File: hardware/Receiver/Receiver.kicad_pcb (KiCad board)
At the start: 4 copper layers, 65 x 42 mm, 120 parts, among them J1 USB_C_Receptacle_USB2.0, J3 JST_PH, J4 Conn_01x04, Q1 2N7002, Q10 NChan, Q11 NChan, Q2 NChan, Q3 NChan, Q4 NChan, Q5 PChan, Q6 PChan, Q7 PChan, Q8 NChan, Q9 NChan, SW1 Reset, SW2 1825027-8, SW3 Boot, U1 TPS22810DRV, U2 DMG6602SVTQ, U3 DMG6602SVTQ, U4 TLV493DA1B6HTSA2, U5 TPS22810DRV, U6 AZ1117-3.3, U7 ESP32-S3-MINI-1-N8

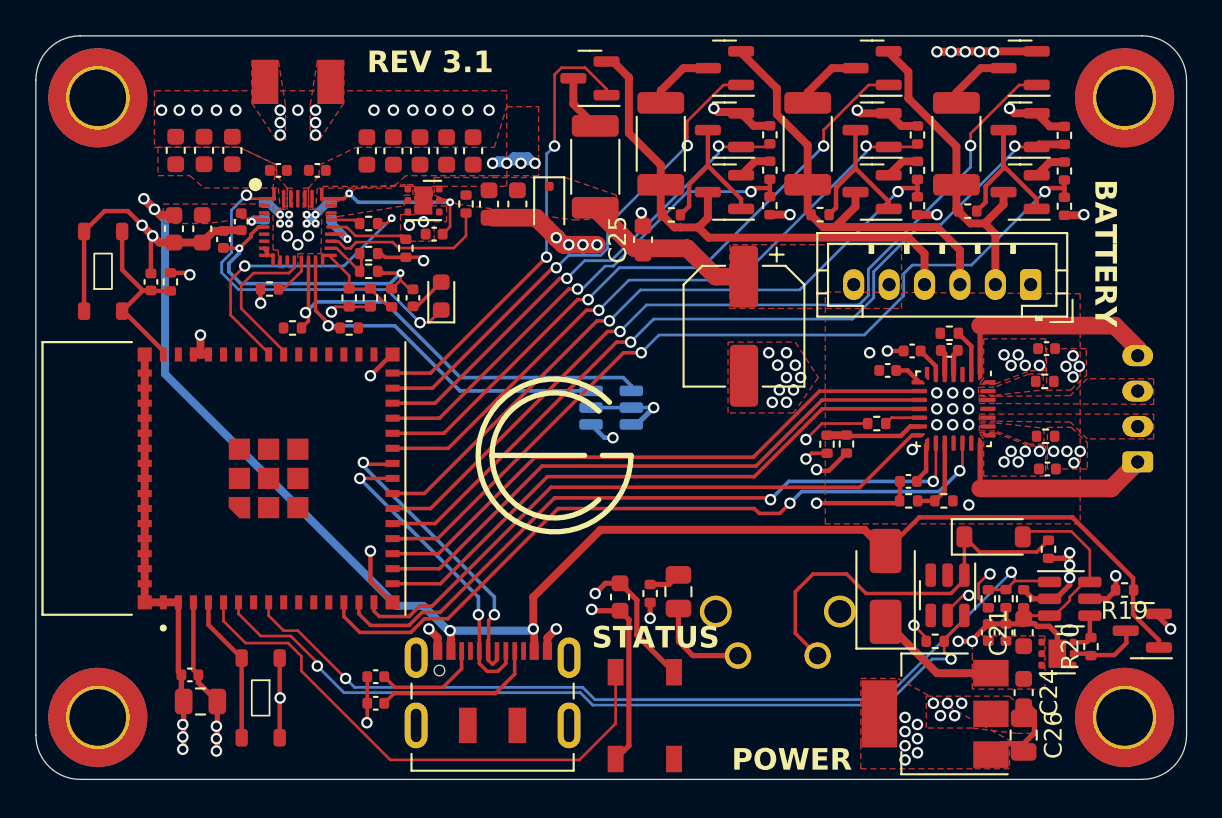
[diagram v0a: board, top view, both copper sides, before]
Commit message: add battery balancing IC
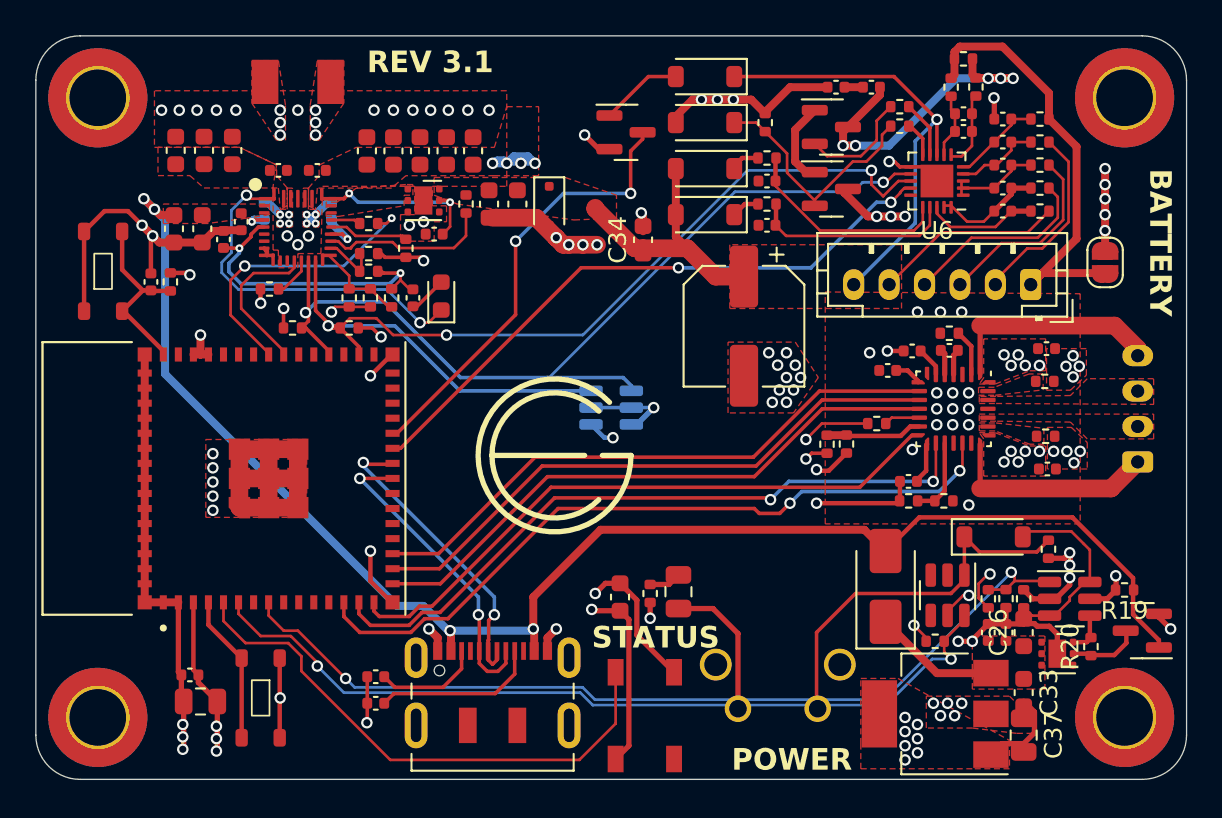
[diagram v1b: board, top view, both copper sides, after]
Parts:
- removed Q10, Q11, Q8, Q9: NChan, Package_TO_SOT_SMD:SOT-23
- removed Q5, Q6, Q7: PChan, Package_TO_SOT_SMD:SOT-23
- removed the R34 at (152.8, 85.1)
- removed the R35 at (161.1, 85.1)
- removed the R36 at (169.5, 85.1)
- added C21: 220nf, Capacitor_SMD:C_0402_1005Metric, F.Cu at (172.1, 88.9)
- added C22: 220nf, Capacitor_SMD:C_0402_1005Metric, F.Cu at (172.1, 87.6)
- added C23: 220nf, Capacitor_SMD:C_0402_1005Metric, F.Cu at (172.1, 86.3)
- added C24: 220nf, Capacitor_SMD:C_0402_1005Metric, F.Cu at (172.1, 85.0)
- added C25: 220nf, Capacitor_SMD:C_0402_1005Metric, F.Cu at (172.1, 83.7)
- added C28: 100p, Capacitor_SMD:C_0402_1005Metric, F.Cu at (169.9, 84.4)
- added C29: 0.1u, Capacitor_SMD:C_0402_1005Metric, F.Cu at (169.9, 83.4)
- added C30: 1u, Capacitor_SMD:C_0402_1005Metric, F.Cu at (158.8, 89.7)
- added C32: 1u, Capacitor_SMD:C_0402_1005Metric, F.Cu at (158.8, 87.2)
- added C35: 0.1u, Capacitor_SMD:C_0402_1005Metric, F.Cu at (164.7, 81.9)
- added C36: 0.1u, Capacitor_SMD:C_0402_1005Metric, F.Cu at (162.7, 81.9)
- added D10: 1N4148WQ-13-F, Diode_SMD:D_SOD-123, F.Cu at (155.3, 83.9)
- added D7: 1N4148WQ-13-F, Diode_SMD:D_SOD-123, F.Cu at (155.3, 89.1)
- added D8: 1N4148WQ-13-F, Diode_SMD:D_SOD-123, F.Cu at (155.3, 86.5)
- added D9: 1N4148WQ-13-F, Diode_SMD:D_SOD-123, F.Cu at (155.3, 81.3)
- added JP1: BQ76905_Bypass, Jumper:SolderJumper-2_P1.3mm_Open_RoundedPad1.0x1.5mm, F.Cu at (177.9, 91.8)
- added U6: ~, Package_DFN_QFN:UQFN-20-1EP_3x3mm_P0.4mm_EP1.85x1.85mm, F.Cu at (168.4, 87.2)
- Q2, Q3: value NChan -> NMOS
- Q4: value NChan -> PMOS
- R21, R22, R23, R24, R25: value 100k -> 10
- R26, R28: value 100k -> 100
- R27: value 282k -> 1m
- R29: value 155k -> 100
- R30: value 100k -> 0
- R31: value 28k -> 5.1k
- R32: value 100k -> 5.1k
- R33: value 400 -> 100k; footprint Resistor_SMD:R_2010_5025Metric -> Resistor_SMD:R_0402_1005Metric
- moved Q4 22.3 mm to (150.8, 84.5), turned to 0 degrees
- moved R24 21.2 mm to (174.2, 85.0), turned to 180 degrees
- moved R21 15.9 mm to (174.2, 88.9), turned to 180 degrees
- moved R25 13.5 mm to (174.2, 83.7), turned to 180 degrees
- moved R27 12.6 mm to (169.9, 80.3), turned to 0 degrees
- moved R32 10.3 mm to (166.3, 84.1), turned to 180 degrees
- moved R31 9.99 mm to (166.3, 83.0), turned to 180 degrees
- moved R33 9.92 mm to (158.7, 83.9), turned to -90 degrees
- moved R30 8.92 mm to (158.8, 85.9), turned to 0 degrees
- moved R22 7.54 mm to (174.2, 87.6), turned to 180 degrees
- moved R26 7.06 mm to (169.2, 81.9), turned to 90 degrees
- moved Q2 6.04 mm to (162.4, 84.2), turned to 0 degrees
- moved R29 5.75 mm to (170.6, 81.9), turned to 90 degrees
- moved Q3 4.04 mm to (162.4, 87.7), turned to 0 degrees
- moved SW3 3.00 mm to (157.2, 117.0)
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- renumbered C21 to C26, C22 to C27, C23 to C31, C24 to C33, C25 to C34, C26 to C37, C30 to C38, C27 to C39, C28 to C40, C29 to C41, C31 to C42, C32 to C43, C35 to C44, C34 to C45, C36 to C46, C33 to C47, R39 to R34, R40 to R35, R41 to R36, R46 to R37, R47 to R38, R37 to R39, R44 to R40, R45 to R41, R38 to R42, R42 to R43, R43 to R44, SW3 to SW2, SW2 to SW3, U6 to U7, U7 to U8
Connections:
- BQ25792RQMR1 pad 16: /TS -> Net-(BQ25792RQMR1-TS)
- J3 pad 1: GND -> /BAT_C0
- J3 pad 6: /TC -> /TS
- Q2 pad 1: /M2 -> Net-(Q2-D)
- Q2 pad 2: GND -> Net-(Q2-G)
- Q2 pad 3: Net-(Q2-D) -> Net-(Q2-S)
- Q3 pad 1: /M3 -> Net-(Q2-D)
- Q3 pad 2: GND -> Net-(D10-K)
- Q3 pad 3: Net-(Q3-D) -> GND
- Q4 pad 1: /M4 -> Net-(D9-A)
- Q4 pad 2: GND -> +3.3V
- Q4 pad 3: Net-(Q4-D) -> /WAKE
- R13 pad 2: /TS -> Net-(BQ25792RQMR1-TS)
- R14 pad 1: /TS -> Net-(BQ25792RQMR1-TS)
- R16 pad 1: /TS -> Net-(BQ25792RQMR1-TS)
- R21 pad 1: /M2 -> /BAT+
- R21 pad 2: GND -> /VC4
- R22 pad 1: /M3 -> /BAT_C3
- R22 pad 2: GND -> /VC3
- R23 pad 1: /M4 -> /BAT_C2
- R23 pad 2: GND -> /VC2
- R24 pad 1: /BAT_C3 -> /BAT_C1
- R24 pad 2: Net-(Q2-D) -> /VC1
- R25 pad 1: /BAT_C2 -> /BAT_C0
- R25 pad 2: Net-(Q3-D) -> /VC0
- R26 pad 1: /BAT_C1 -> Net-(U6-SRN)
- R26 pad 2: Net-(Q4-D) -> /BAT_C0
- R27 pad 1: Net-(Q5-S) -> /BAT_C0
- R27 pad 2: /S2 -> Net-(Q2-S)
- R28 pad 1: /S2 -> Net-(D7-K)
- R28 pad 2: GND -> Net-(U6-BAT)
- R29 pad 2: /S3 -> Net-(Q2-S)
- R30 pad 1: /S3 -> Net-(D8-K)
- R30 pad 2: GND -> Net-(U6-REGSRC)
- R31 pad 2: /S4 -> Net-(Q2-G)
- R32 pad 1: /S4 -> Net-(U6-CHG)
- R32 pad 2: GND -> Net-(D10-K)
- R33 pad 1: /BAT+ -> GND
- R33 pad 2: Net-(Q8-D) -> Net-(D10-K)
- U8 pad 16: /MS3 -> unconnected-(U8-IO12-Pad16)
- U8 pad 17: /MS2 -> unconnected-(U8-IO13-Pad17)
- U8 pad 18: /MS1 -> unconnected-(U8-IO14-Pad18)
- U8 pad 19: /S4 -> /MS3
- U8 pad 20: /M4 -> /MS2
- U8 pad 21: /C4 -> /MS1
- U8 pad 22: /S3 -> unconnected-(U8-IO18/DAC2-Pad22)
- U8 pad 25: /M3 -> /ALERT
- U8 pad 26: /C3 -> /WAKE
- U8 pad 27: /S2 -> unconnected-(U8-IO47-Pad27)
- U8 pad 28: /M2 -> unconnected-(U8-IO33-Pad28)
- U8 pad 29: /C2 -> unconnected-(U8-IO34-Pad29)
- U8 pad 30: /C1 -> unconnected-(U8-IO48-Pad30)
- U8 pad 32: unconnected-(U7-IO36-Pad32) -> /SDA
- U8 pad 33: unconnected-(U7-IO37-Pad33) -> /SCL
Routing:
- net /C4: track 48.4 -> 0.00 mm, vias 2 -> 0
- net /M4: track 47.9 -> 0.00 mm, vias 2 -> 0
- net /S4: track 47.8 -> 0.00 mm, vias 2 -> 0
- net /SDA: track 21.0 -> 61.8 mm, vias 1 -> 3
- net /S3: track 37.8 -> 0.00 mm, vias 2 -> 0
- net /M3: track 37.0 -> 0.00 mm, vias 2 -> 0
- net /C3: track 36.7 -> 0.00 mm, vias 2 -> 0
- net /ALERT: track 0.00 -> 35.5 mm, vias 0 -> 2
- net /C2: track 28.5 -> 0.00 mm, vias 2 -> 0
- net /S2: track 27.7 -> 0.00 mm, vias 2 -> 0
- net /M2: track 27.7 -> 0.00 mm, vias 2 -> 0
- net /SCL: track 24.9 -> 52.4 mm, vias 1 -> 2
- net GND: track 131.8 -> 158.2 mm, vias 94 -> 104
- net /C1: track 25.9 -> 0.00 mm, vias 2 -> 0
- net /WAKE: track 0.00 -> 25.2 mm, vias 0 -> 2
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
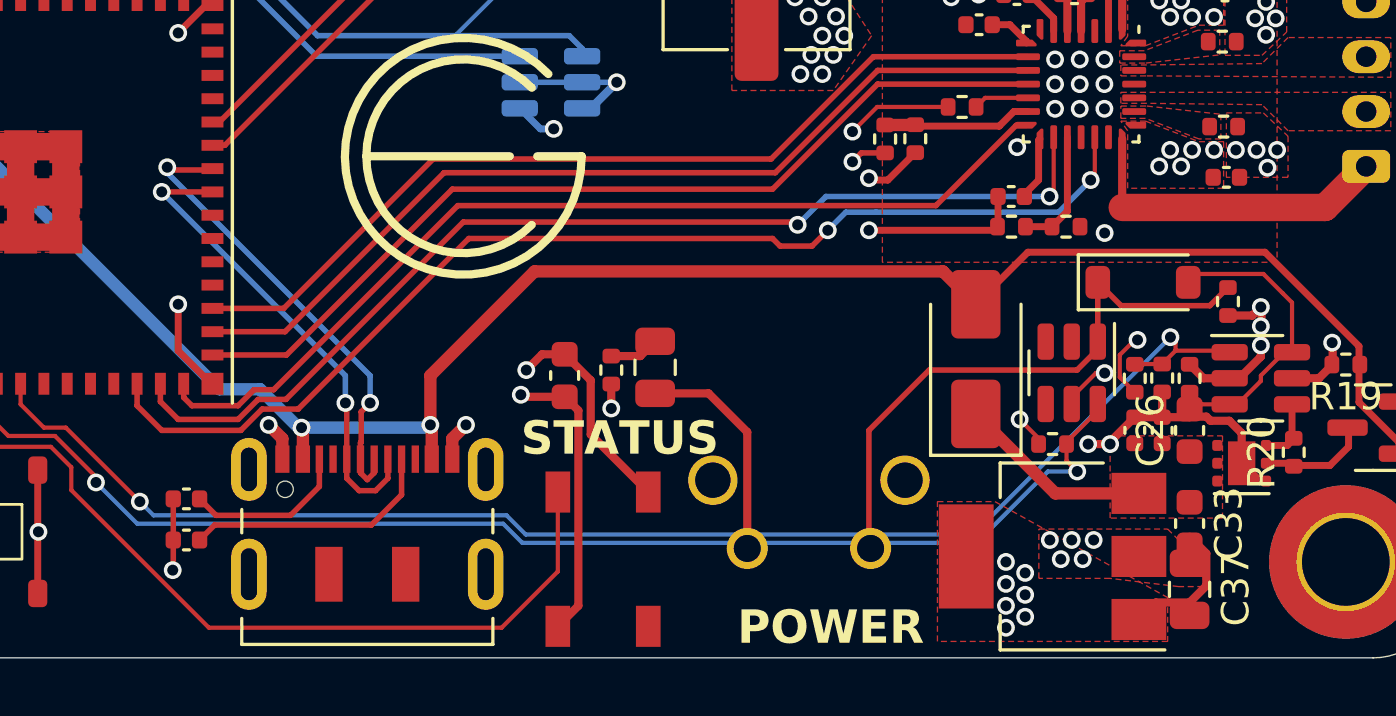
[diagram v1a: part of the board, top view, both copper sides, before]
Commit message: add tvs diodes
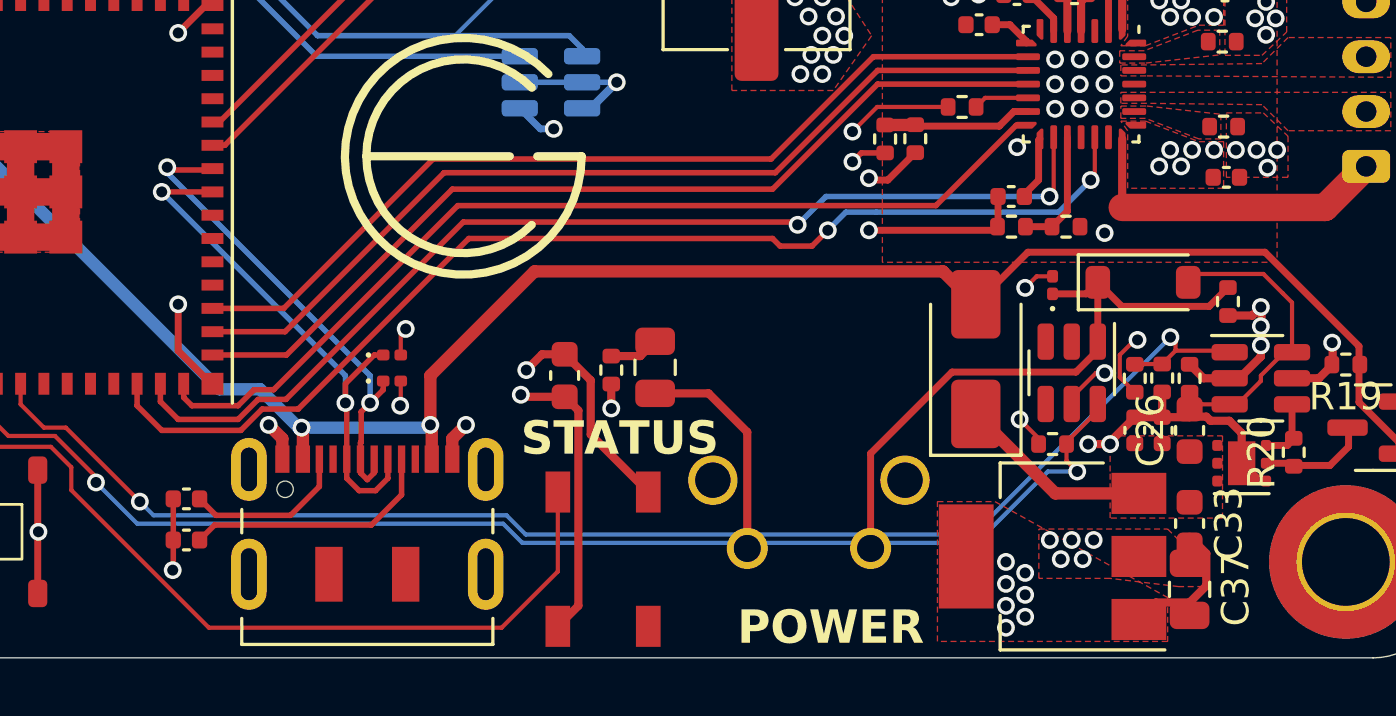
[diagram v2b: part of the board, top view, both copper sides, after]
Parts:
- added D11: ESD051-1F4, Diode_SMD:D_0201_0603Metric, F.Cu at (144.2, 110.0)
- added D12: ESD051-1F4, Diode_SMD:D_0201_0603Metric, F.Cu at (144.2, 110.9)
- added D13: ESD051-1F4, Diode_SMD:D_0201_0603Metric, F.Cu at (168.3, 107.4)
- U6: value ~ -> BQ76905
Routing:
- net GND: track 158.2 -> 161.3 mm, vias 104 -> 107
- net /D-: track 17.7 -> 20.2 mm
- net Net-(D13-A1): track 21.7 -> 23.0 mm
- net /D+: track 17.3 -> 18.3 mm

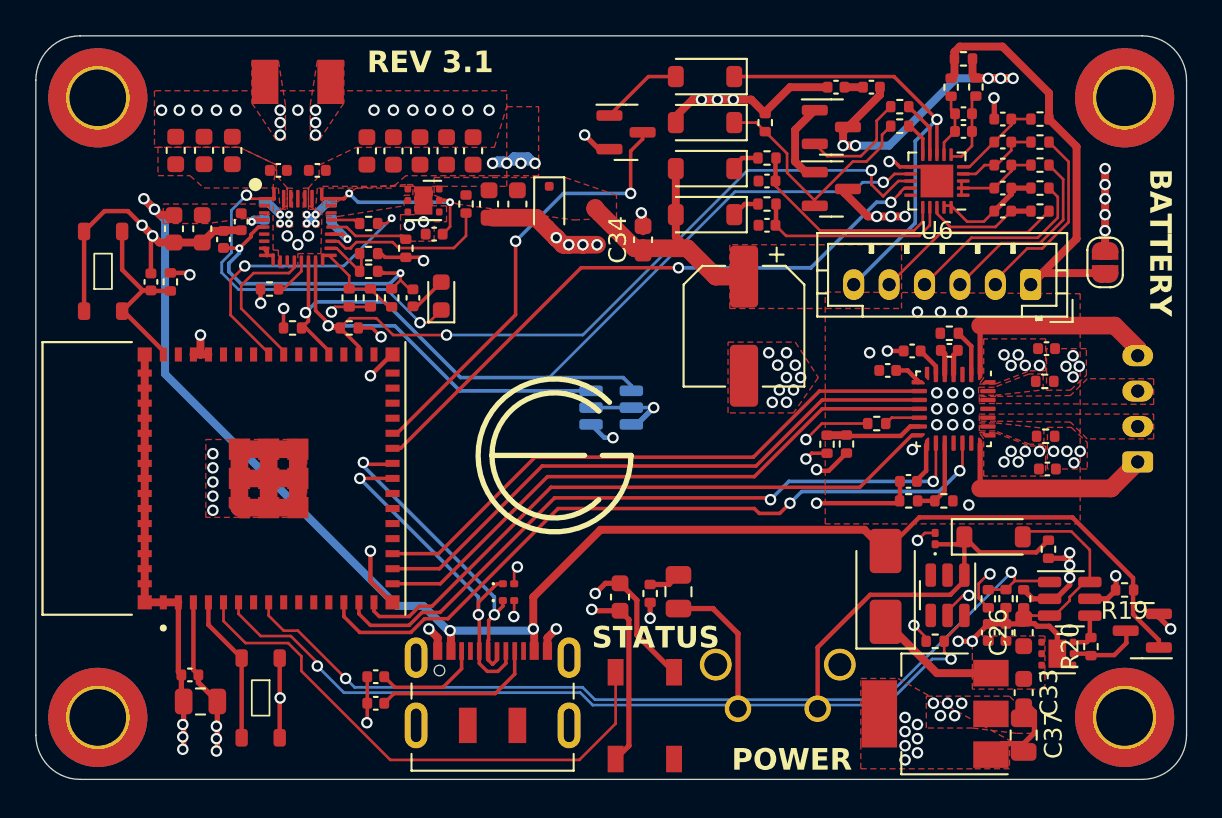
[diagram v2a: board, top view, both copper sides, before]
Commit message: add stitching vias
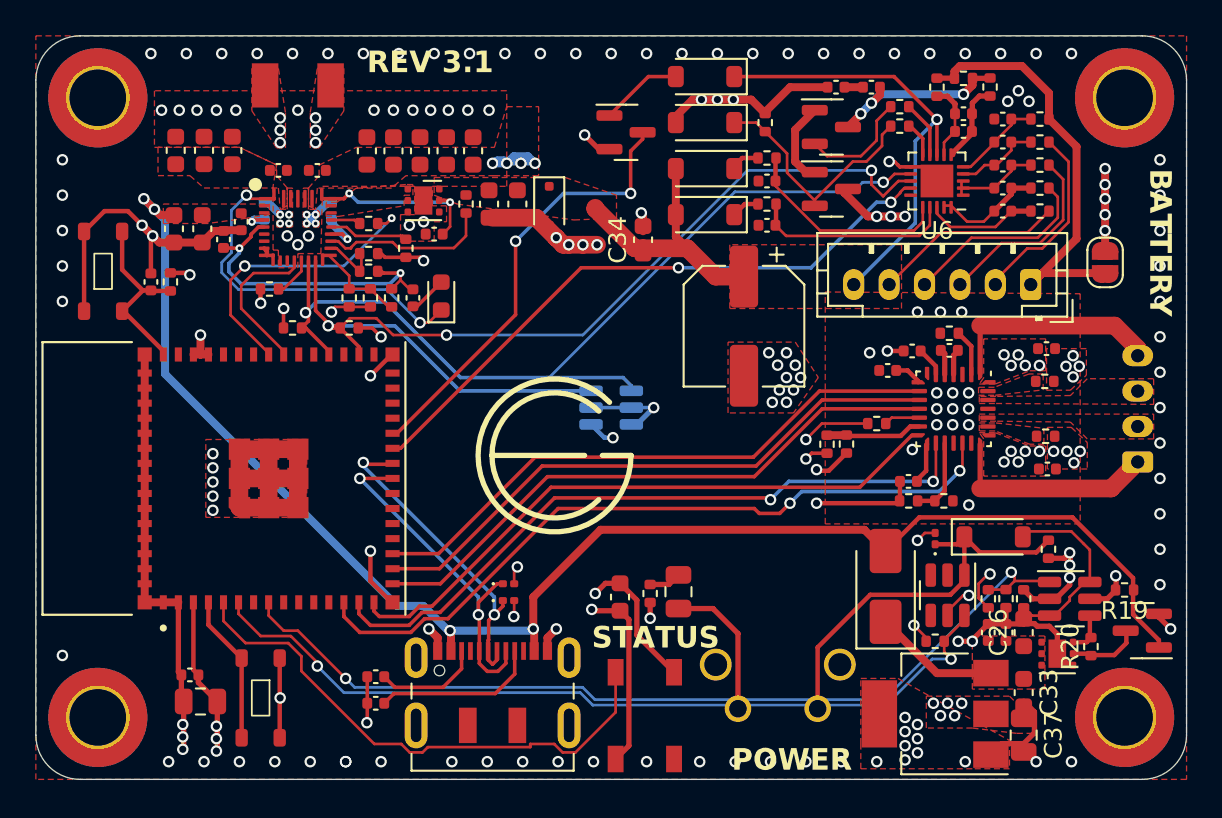
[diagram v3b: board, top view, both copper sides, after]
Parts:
- moved R27 1.10 mm to (169.9, 81.4)
- moved R29 0.80 mm to (171.4, 81.9)
- moved R26 0.80 mm to (168.4, 81.9)
- moved L1 0.20 mm to (132.3, 81.8)
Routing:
- net Net-(Q2-S): track 19.4 -> 10.5 mm, vias 5 -> 3
- net GND: track 161.3 -> 159.9 mm, vias 107 -> 174
- net Net-(U6-SRN): track 3.75 -> 4.43 mm
- net /BAT_C0: track 25.1 -> 24.5 mm
- net (no net): vias 0 -> 4

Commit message: update emc
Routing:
- net GND: vias 174 -> 222
- added copper zone on B.Cu, net GND

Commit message: create bom
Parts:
- moved C33 1.22 mm to (174.5, 115.9), turned to 0 degrees
- moved C37 0.63 mm to (173.9, 118.7)
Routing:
- net GND: track 159.9 -> 144.8 mm, vias 222 -> 223
- net /BAT_C1: track 10.7 -> 11.7 mm
- net /BAT_C0: track 24.5 -> 25.5 mm
- net Net-(U6-BAT): track 11.5 -> 12.5 mm
- net /VIN: track 7.15 -> 8.00 mm
- net /BAT_C2: track 10.8 -> 11.6 mm
- net /SHUTDOWN: track 51.9 -> 51.2 mm
- net /STAT: track 20.1 -> 20.8 mm
- net Net-(U6-REGSRC): track 12.1 -> 12.7 mm
- net /SW: track 47.3 -> 46.7 mm
- net /SW1: track 10.5 -> 11.0 mm

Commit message: PCB revision
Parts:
- removed C19, C20: 10u, Capacitor_SMD:C_0603_1608Metric
- added D14: TVN3V3B1S, Diode_SMD:D_0402_1005Metric, F.Cu at (124.6, 94.8)
- added D15: TVN3V3B1S, Diode_SMD:D_0402_1005Metric, F.Cu at (127.9, 113.7)
- added R45: 10k, Resistor_SMD:R_0402_1005Metric, F.Cu at (139.8, 103.6)
- C10, C12, C13, C15, C16, C17, C18, C2, C26, C3, C33, C34, C6: footprint Capacitor_SMD:C_0603_1608Metric -> Capacitor_SMD:C_0805_2012Metric
- D10, D4, D7, D8, D9: footprint Diode_SMD:D_SOD-123 -> Diode_SMD:D_SOD-323
- D11, D12, D13: value ESD051-1F4 -> TVN3V3B1S; footprint Diode_SMD:D_0201_0603Metric -> Diode_SMD:D_0402_1005Metric
- L1: footprint Inductor_SMD:L_Sunlord_MWSA0402S -> Inductor_SMD:L_1008_2520Metric
- R43, R44: footprint Resistor_SMD:R_0402_1005Metric -> Resistor_SMD:R_0603_1608Metric
- moved U2 2.55 mm to (177.7, 109.0)
- moved R20 2.10 mm to (177.0, 111.4), turned to 180 degrees
- moved D5 1.98 mm to (147.8, 87.1), turned to 90 degrees
- moved R19 1.77 mm to (180.7, 109.8), turned to 90 degrees
- moved C15 1.58 mm to (139.2, 85.0)
- moved U5 1.57 mm to (176.6, 113.2)
- moved D4 1.20 mm to (172.8, 107.2)
- moved R17 1.20 mm to (174.5, 110.7), turned to 180 degrees
- moved C17 1.03 mm to (137.1, 85.0)
- moved R9 1.02 mm to (174.5, 109.0), turned to 180 degrees
- moved C18 0.92 mm to (145.6, 88.7)
- moved C13 0.78 mm to (141.3, 85.0)
- moved C26 0.76 mm to (174.0, 113.0)
- moved C3 0.75 mm to (124.5, 89.9)
- moved C16 0.45 mm to (143.5, 88.7)
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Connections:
- U8 pad 22: unconnected-(U8-IO18/DAC2-Pad22) -> Net-(U8-IO18/DAC2)
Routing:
- net GND: track 144.8 -> 133.4 mm, vias 223 -> 222
- net /VUSB: track 86.7 -> 90.7 mm, vias 4 -> 3
- net /VSYS: track 72.6 -> 76.4 mm, vias 7 -> 10
- net /SHUTDOWN: track 51.2 -> 53.7 mm, vias 2 -> 3
- net /VIN: track 8.00 -> 10.3 mm
- net Net-(U2-D2): track 2.40 -> 4.61 mm
- net Net-(U8-IO18/DAC2): track 0.00 -> 2.16 mm
- net +3.3V: track 43.2 -> 45.2 mm
- net /CNTRL: track 11.5 -> 10.4 mm
- net /MS3: track 33.8 -> 32.8 mm
- net /MS2: track 33.7 -> 32.7 mm
- net /SCL: track 52.4 -> 53.3 mm
- net /ESP_EN: track 10.5 -> 11.3 mm
- net /MS1: track 33.6 -> 32.7 mm
- net /TS: track 25.8 -> 26.5 mm
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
